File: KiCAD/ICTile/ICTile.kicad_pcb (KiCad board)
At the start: 2 copper layers, 59 x 23 mm, 12 parts, among them J1 Conn_02x08_Counter_Clockwise, J2 Conn_02x08_Odd_Even, J3 Conn_02x08_Odd_Even, J4 Conn_02x08_Odd_Even, J5 Conn_02x08_Odd_Even, J6 Conn_02x02_Odd_Even, J7 Conn_02x02_Odd_Even

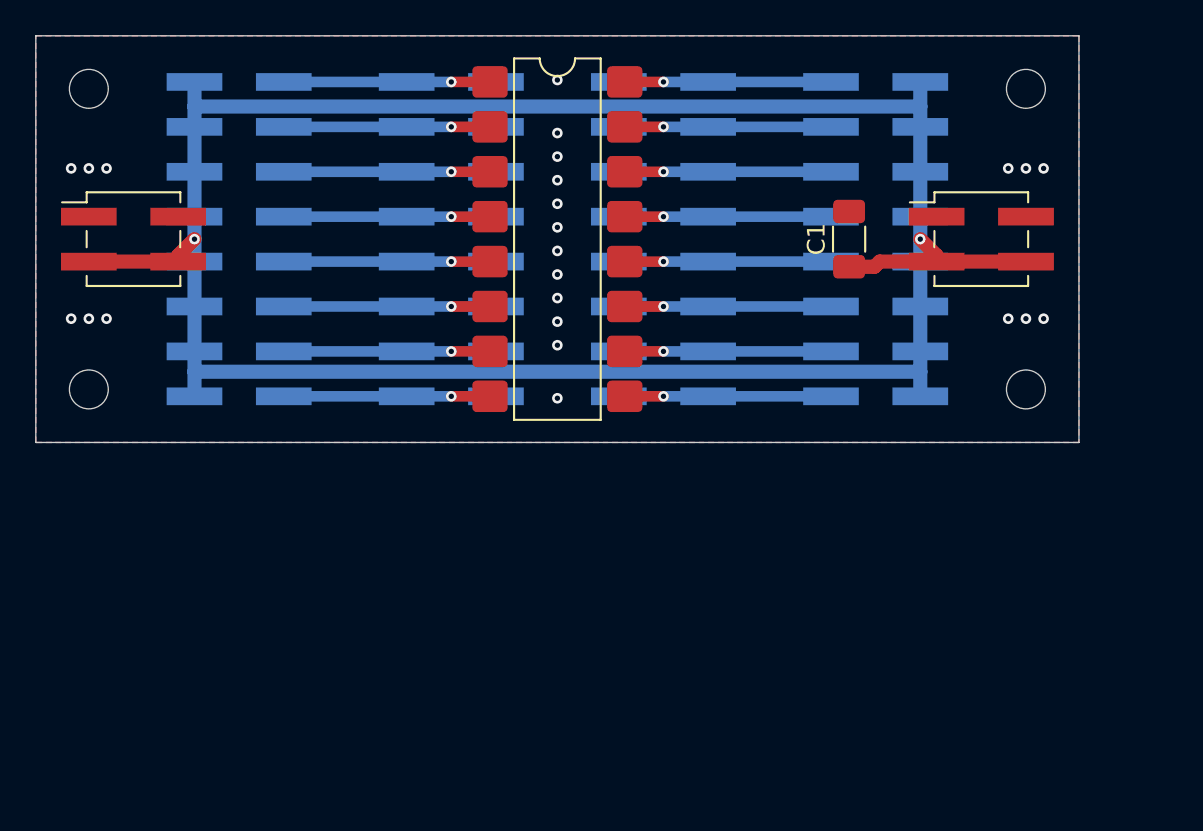
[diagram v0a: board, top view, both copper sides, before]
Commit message: Redesign to use 0 Ohm Resistor Jumpers instead of Pin Header Jumpers
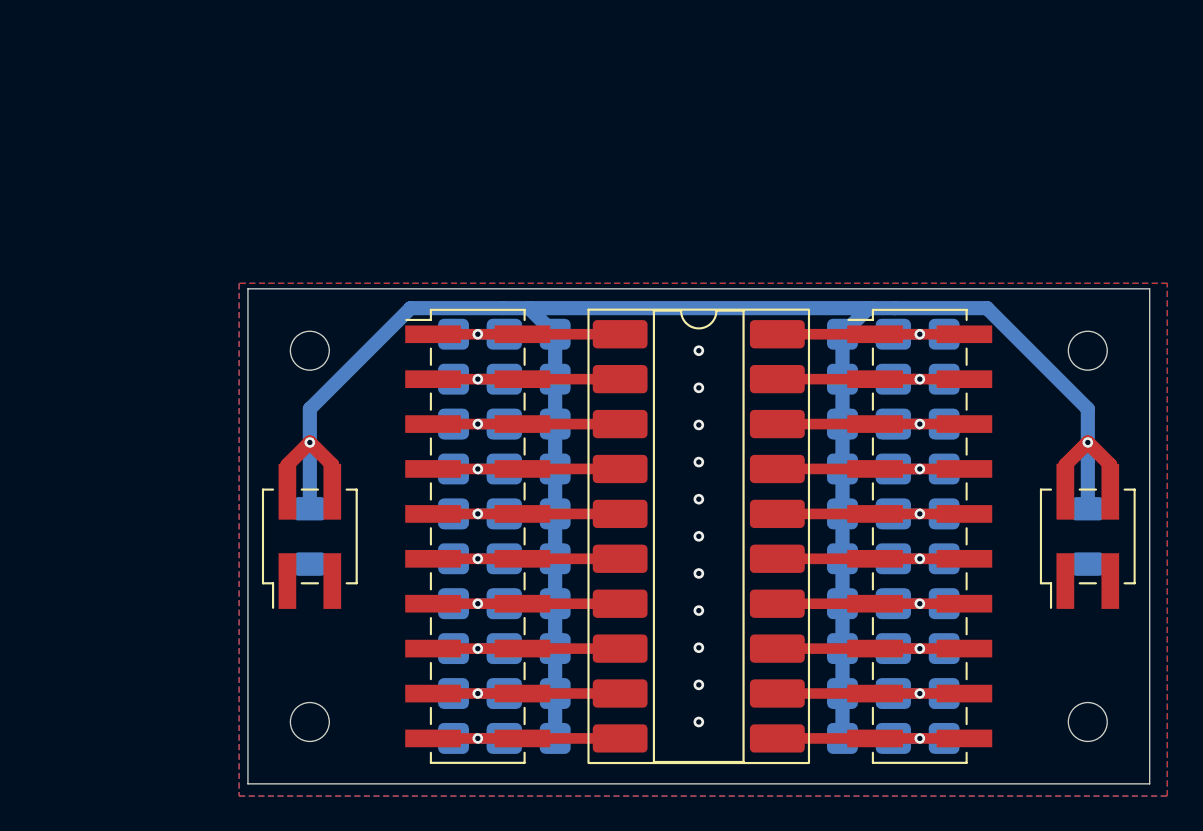
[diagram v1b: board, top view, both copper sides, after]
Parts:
- removed J4, J5: Conn_02x08_Odd_Even, Connector_PinHeader_2.54mm:PinHeader_2x08_P2.54mm_Vertical_SMD
- added C2: 10u, Capacitor_SMD:C_1206_3216Metric_Pad1.33x1.80mm_HandSolder, B.Cu at (145.0, 92.8)
- added JP1: SolderJumper_3_Open, Customs:1206_3Way_Open, B.Cu at (112.0, 81.4)
- added JP10: SolderJumper_3_Open, Customs:1206_3Way_Open, B.Cu at (112.0, 104.2)
- added JP11: SolderJumper_3_Open, Customs:1206_3Way_Open, B.Cu at (134.0, 81.4)
- added JP12: SolderJumper_3_Open, Customs:1206_3Way_Open, B.Cu at (134.0, 83.9)
- added JP13: SolderJumper_3_Open, Customs:1206_3Way_Open, B.Cu at (134.0, 86.5)
- added JP14: SolderJumper_3_Open, Customs:1206_3Way_Open, B.Cu at (134.0, 89.0)
- added JP15: SolderJumper_3_Open, Customs:1206_3Way_Open, B.Cu at (134.0, 91.5)
- added JP16: SolderJumper_3_Open, Customs:1206_3Way_Open, B.Cu at (134.0, 94.1)
- added JP17: SolderJumper_3_Open, Customs:1206_3Way_Open, B.Cu at (134.0, 96.6)
- added JP18: SolderJumper_3_Open, Customs:1206_3Way_Open, B.Cu at (134.0, 99.2)
- added JP19: SolderJumper_3_Open, Customs:1206_3Way_Open, B.Cu at (134.0, 101.7)
- added JP2: SolderJumper_3_Open, Customs:1206_3Way_Open, B.Cu at (112.0, 83.9)
- added JP20: SolderJumper_3_Open, Customs:1206_3Way_Open, B.Cu at (134.0, 104.2)
- added JP3: SolderJumper_3_Open, Customs:1206_3Way_Open, B.Cu at (112.0, 86.5)
- added JP4: SolderJumper_3_Open, Customs:1206_3Way_Open, B.Cu at (112.0, 89.0)
- added JP5: SolderJumper_3_Open, Customs:1206_3Way_Open, B.Cu at (112.0, 91.5)
- added JP6: SolderJumper_3_Open, Customs:1206_3Way_Open, B.Cu at (112.0, 94.1)
- added JP7: SolderJumper_3_Open, Customs:1206_3Way_Open, B.Cu at (112.0, 96.6)
- added JP8: SolderJumper_3_Open, Customs:1206_3Way_Open, B.Cu at (112.0, 99.2)
- added JP9: SolderJumper_3_Open, Customs:1206_3Way_Open, B.Cu at (112.0, 101.7)
- C1: moved to B.Cu
- J1: value Conn_02x08_Counter_Clockwise -> Conn_02x10_Counter_Clockwise; footprint Package_DIP:SMDIP-16_W7.62mm -> Package_DIP:DIP-20_W8.89mm_SMDSocket_LongPads
- J2, J3: value Conn_02x08_Odd_Even -> Conn_02x10_Odd_Even; footprint Connector_PinHeader_2.54mm:PinHeader_2x08_P2.54mm_Vertical_SMD -> Connector_PinHeader_2.54mm:PinHeader_2x10_P2.54mm_Vertical_SMD; moved to F.Cu
- moved H4 59.5 mm to (145.0, 103.3)
- moved H3 58.4 mm to (145.0, 82.3)
- moved J7 56.5 mm to (145.0, 92.8), turned to 90 degrees
- moved H2 44.7 mm to (101.0, 103.3)
- moved H1 43.1 mm to (101.0, 82.3)
- moved J3 42.0 mm to (135.5, 92.8), turned to 0 degrees
- moved J6 41.5 mm to (101.0, 92.8), turned to 90 degrees
- moved C1 34.8 mm to (101.0, 92.8), turned to -90 degrees
- moved J1 18.6 mm to (123.0, 92.8)
- moved J2 16.9 mm to (110.5, 92.8), turned to 0 degrees
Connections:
- J1 pad 1: Net-(J1-Pin_1) -> P0
- J1 pad 10: Net-(J1-Pin_10) -> P9
- J1 pad 11: Net-(J1-Pin_11) -> P19
- J1 pad 12: Net-(J1-Pin_12) -> P18
- J1 pad 13: Net-(J1-Pin_13) -> P17
- J1 pad 14: Net-(J1-Pin_14) -> P16
- J1 pad 15: Net-(J1-Pin_15) -> P15
- J1 pad 16: Net-(J1-Pin_16) -> P14
- J1 pad 2: Net-(J1-Pin_2) -> P1
- J1 pad 3: Net-(J1-Pin_3) -> P2
- J1 pad 4: Net-(J1-Pin_4) -> P3
- J1 pad 5: Net-(J1-Pin_5) -> P4
- J1 pad 6: Net-(J1-Pin_6) -> P5
- J1 pad 7: Net-(J1-Pin_7) -> P6
- J1 pad 8: Net-(J1-Pin_8) -> P7
- J1 pad 9: Net-(J1-Pin_9) -> P8
- J2 pad 1: GND -> P0
- J2 pad 10: Net-(J1-Pin_5) -> P4
- J2 pad 11: GND -> P5
- J2 pad 12: Net-(J1-Pin_6) -> P5
- J2 pad 13: GND -> P6
- J2 pad 14: Net-(J1-Pin_7) -> P6
- J2 pad 15: GND -> P7
- J2 pad 16: Net-(J1-Pin_8) -> P7
- J2 pad 2: Net-(J1-Pin_1) -> P0
- J2 pad 3: GND -> P1
- J2 pad 4: Net-(J1-Pin_2) -> P1
- J2 pad 5: GND -> P2
- J2 pad 6: Net-(J1-Pin_3) -> P2
- J2 pad 7: GND -> P3
- J2 pad 8: Net-(J1-Pin_4) -> P3
- J2 pad 9: GND -> P4
- J3 pad 1: Net-(J1-Pin_1) -> P10
- J3 pad 10: +5V -> P14
- J3 pad 11: Net-(J1-Pin_6) -> P15
- J3 pad 12: +5V -> P15
- J3 pad 13: Net-(J1-Pin_7) -> P16
- J3 pad 14: +5V -> P16
- J3 pad 15: Net-(J1-Pin_8) -> P17
- J3 pad 16: +5V -> P17
- J3 pad 2: +5V -> P10
- J3 pad 3: Net-(J1-Pin_2) -> P11
- J3 pad 4: +5V -> P11
- J3 pad 5: Net-(J1-Pin_3) -> P12
- J3 pad 6: +5V -> P12
- J3 pad 7: Net-(J1-Pin_4) -> P13
- J3 pad 8: +5V -> P13
- J3 pad 9: Net-(J1-Pin_5) -> P14
- J6 pad 2: GND -> +5V
- J6 pad 3: +5V -> GND
- J7 pad 2: GND -> +5V
- J7 pad 3: +5V -> GND
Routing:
- net +5V: track 136.1 -> 123.3 mm
- net P19: track 0.00 -> 12.1 mm, vias 0 -> 1
- net P18: track 0.00 -> 12.1 mm, vias 0 -> 1
- net P17: track 0.00 -> 12.1 mm, vias 0 -> 1
- net P16: track 0.00 -> 12.1 mm, vias 0 -> 1
- net P15: track 0.00 -> 12.1 mm, vias 0 -> 1
- net P14: track 0.00 -> 12.1 mm, vias 0 -> 1
- net P13: track 0.00 -> 12.1 mm, vias 0 -> 1
- net P12: track 0.00 -> 12.1 mm, vias 0 -> 1
- net P11: track 0.00 -> 12.1 mm, vias 0 -> 1
- net P10: track 0.00 -> 12.1 mm, vias 0 -> 1
- net P9: track 0.00 -> 12.1 mm, vias 0 -> 1
- net P8: track 0.00 -> 12.1 mm, vias 0 -> 1
- net P7: track 0.00 -> 12.1 mm, vias 0 -> 1
- net P6: track 0.00 -> 12.1 mm, vias 0 -> 1
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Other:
- board size 59 x 23 mm -> 51 x 28 mm
- board text added: "+5V"
- board text added: "1"
- board text added: "10"
- board text added: "7"
- board text added: "GND"
